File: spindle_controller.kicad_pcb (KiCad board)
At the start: 2 copper layers, 62 x 112 mm, 67 parts, among them J1 VAC 230V, J2 AUX/CONTROL, J3 ICP, J4 Load output, J5 CONN_01X03, J6 CONN_01X03, J7 GND_JUMPER, J8 VCC_JUMPER, Q1 2N3904, SW1 Rotary_Encoder_Switch, T1 230 - 6VAC (Spitznagel SPK 01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, U1 LM2940CT-5.0, U2 ATMEGA328P-PU, U3 PC817, U4 MOC3020M, U5 TCRT5000, U6 LT1117-5, Y1 16MHz

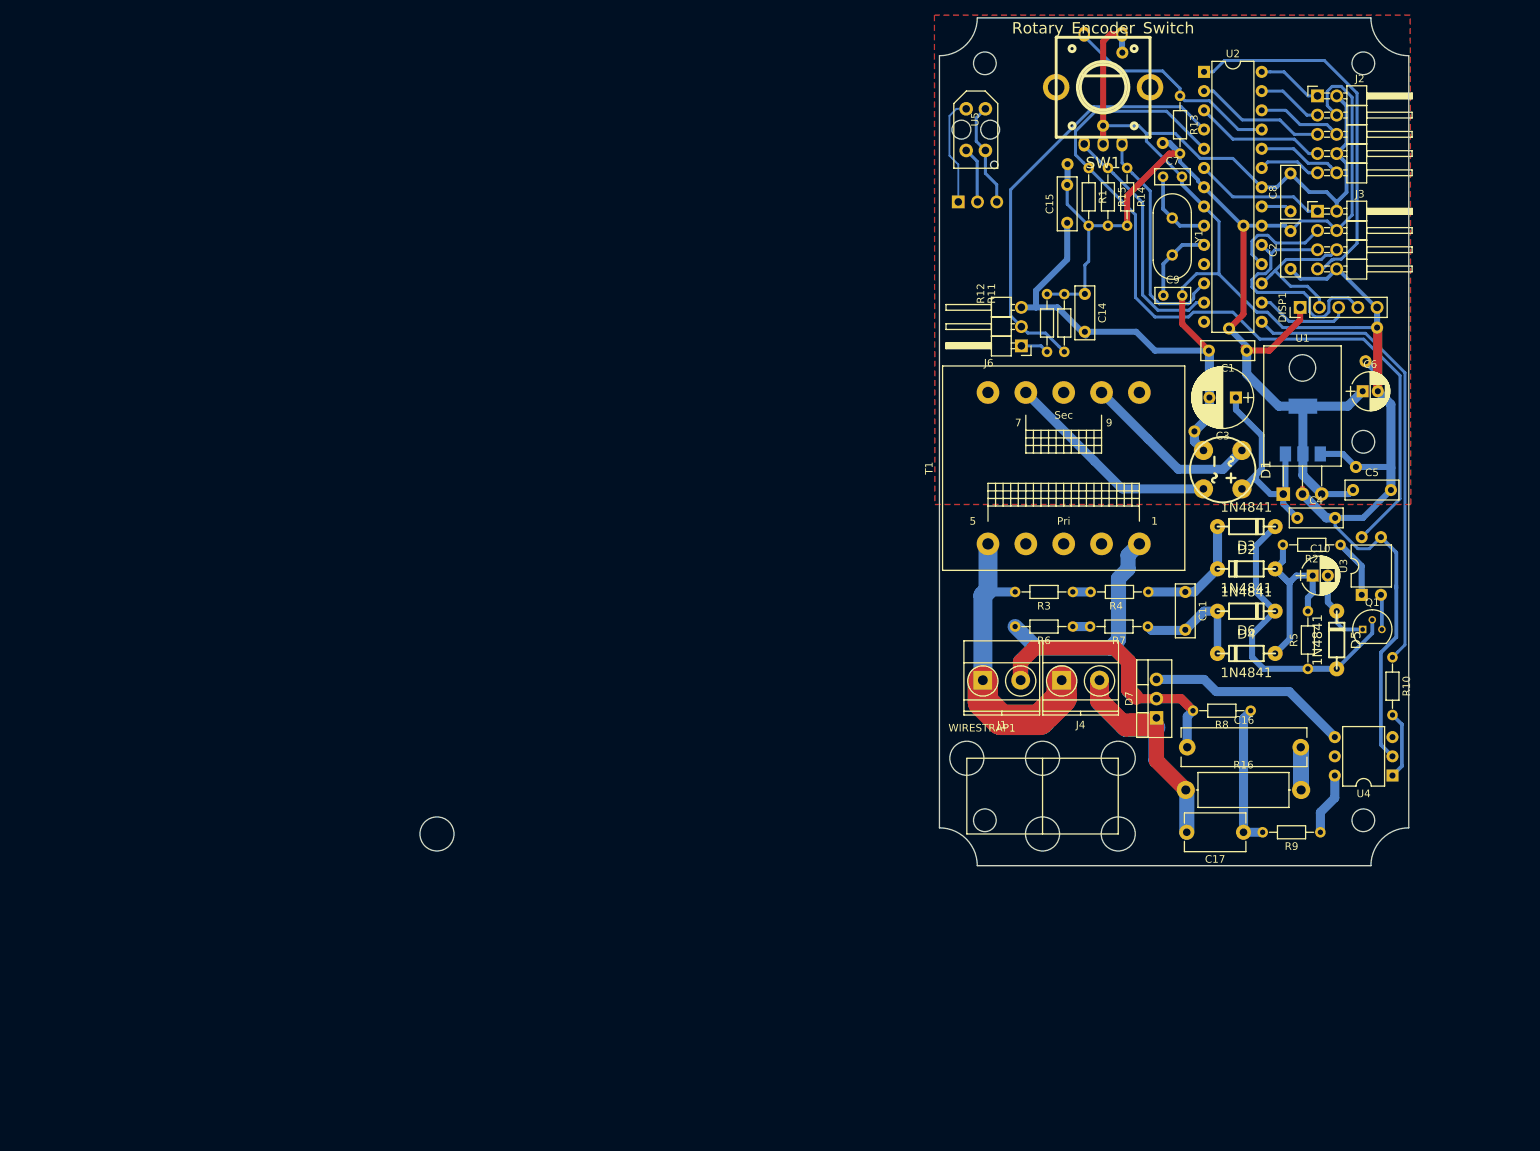
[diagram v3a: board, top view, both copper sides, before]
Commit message: Add breakaway board for optical sensor, general board updates, dissipation planes, screw clearances and silkscreen
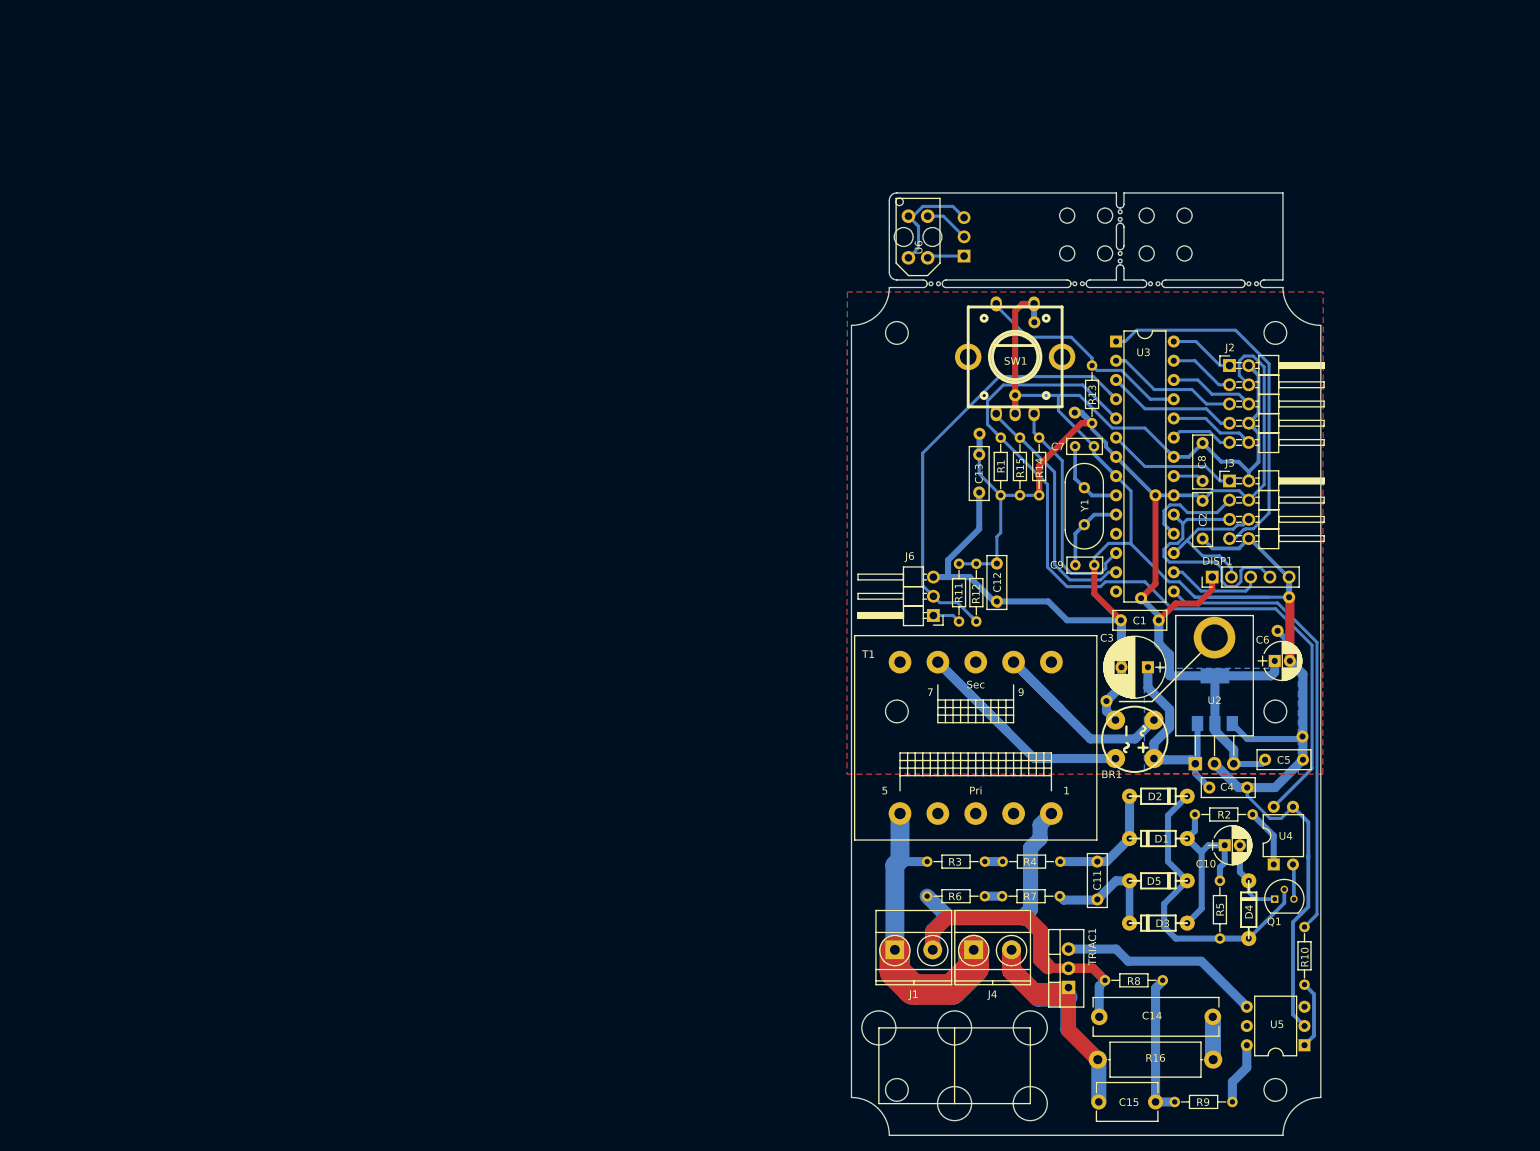
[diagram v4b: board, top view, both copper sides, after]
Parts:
- removed the U1 at (115.9, 77.4)
- added U2: LM2940CT-5.0, iotta_footprints:TO-220_Horizontal_connected_tab, F.Cu at (104.3, 113.0)
- CASE1: footprint iotta_footprints:CASE_KEMO_G085N -> iotta_footprints:CASE_KEMO_G085N+BREAKAWAY_SENSOR
- WIRESTRAP1: footprint iotta_footprints:WireStrap_2X -> iotta_footprints:WireStrap_2X_5HOLES
- moved C11 37.5 mm to (91.3, 125.9)
- moved C14 37.5 mm to (91.6, 146.4)
- moved C15 37.5 mm to (99.0, 157.7)
- moved C2 37.5 mm to (105.2, 83.2)
- moved C3 37.5 mm to (98.0, 100.2)
- moved C5 37.5 mm to (113.5, 112.5)
- moved CASE1 37.5 mm to (54.8, 166.1)
- moved D1 37.5 mm to (99.4, 122.9)
- moved DISP1 37.5 mm to (106.5, 88.3)
- moved J1 37.5 mm to (64.6, 137.6)
- moved J4 37.5 mm to (75.0, 137.6)
- moved J6 37.5 mm to (69.7, 93.4)
- moved J7 37.5 mm to (92.5, 104.7)
- moved J7 37.5 mm to (116.6, 91.0)
- moved J7 37.5 mm to (80.5, 64.3)
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- renumbered D1 to BR1, C14 to C12, C15 to C13, C16 to C14, C17 to C15, D2 to D1, D3 to D2, D4 to D3, D5 to D4, D6 to D5, D7 to TRIAC1, U6 to U1, U2 to U3, U3 to U4, U4 to U5, U5 to U6
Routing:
- net Net-(BR1-Pad3): track 28.7 -> 41.6 mm
- net GND: track 307.7 -> 319.2 mm
- net Net-(J5-Pad1): track 14.4 -> 4.91 mm
- net Net-(BR1-Pad2): track 23.8 -> 32.5 mm
- net /ZCROSS_PULSE: track 108.6 -> 114.2 mm
- net Net-(J5-Pad3): track 13.9 -> 18.2 mm
- net VCC: track 166.7 -> 169.7 mm
- net /VAC_L: track 95.5 -> 98.4 mm
- net /ROT_PULSE: track 57.1 -> 59.6 mm
- net Net-(C15-Pad2): track 80.3 -> 82.1 mm
- net /MOSI: track 20.3 -> 22.0 mm
- net Net-(J5-Pad2): track 7.44 -> 5.94 mm
- net /TRIAC_DRIVE: track 60.0 -> 61.3 mm
- net /PC3: track 11.2 -> 12.4 mm
- net /PD7: track 11.2 -> 12.4 mm
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- added copper zone on B.Cu, net VCC
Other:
- board size 62 x 112 mm -> 62 x 124.5 mm
- board text removed: "Liggende TO220 voor 7805. screw to board, sink via's Angled connectors aan achterkant huis INpassen sensor break-off board. Aanpassen C17 footpirnt naar Y2 ceramic"

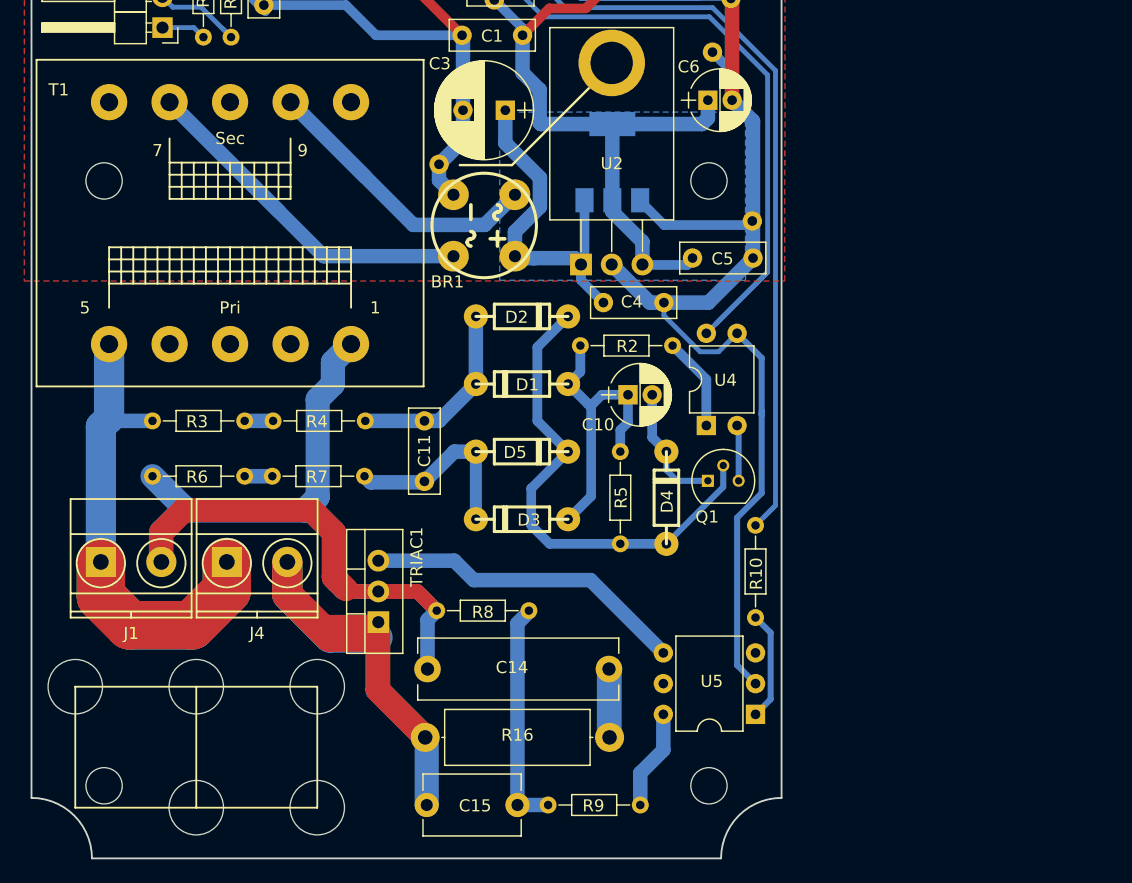
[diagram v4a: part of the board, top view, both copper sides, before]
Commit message: Trying to __squeeze__ in a heatsink for the TRIAC, routing suffers.
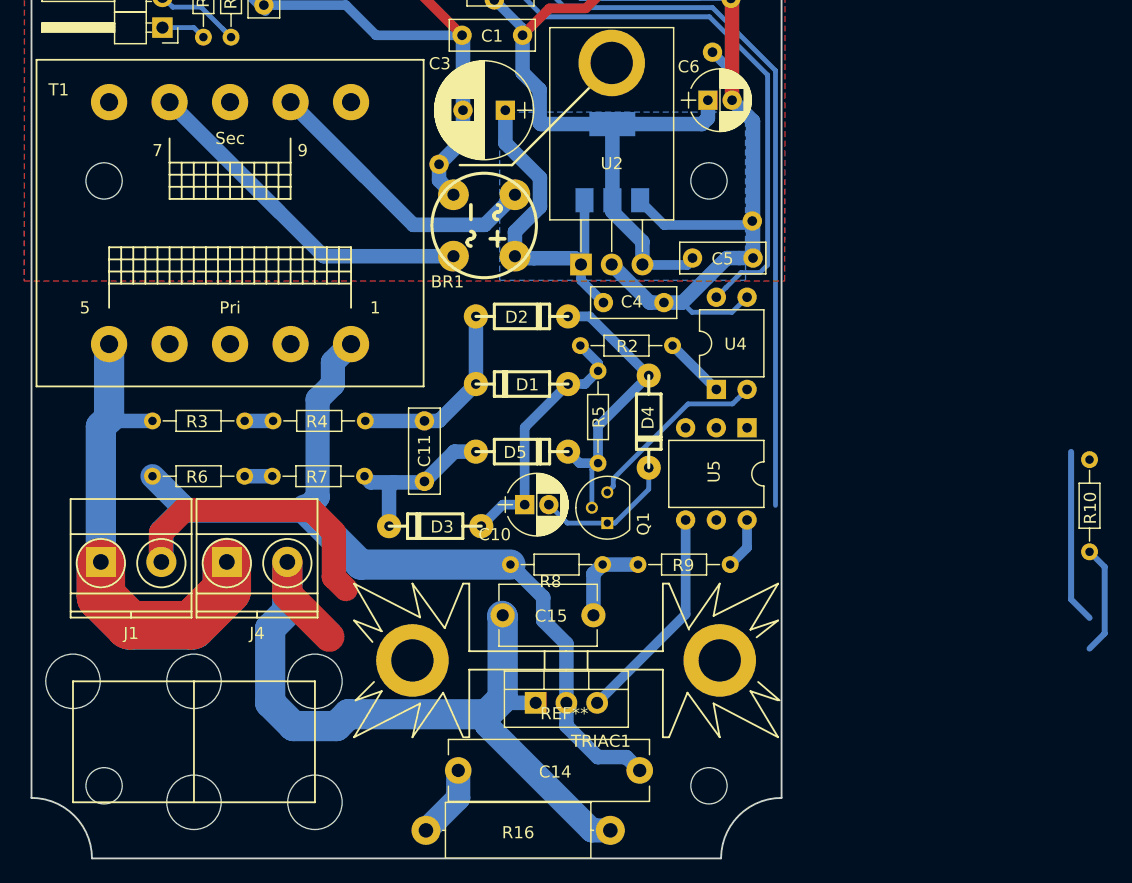
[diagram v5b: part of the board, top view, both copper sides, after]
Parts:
- added REF**: Heatsink_Fischer_SK104-STCB_35x13mm__2xDrill3.5mm_ScrewM3, Heatsinks:Heatsink_Fischer_SK104-STCB_35x13mm__2xDrill3.5mm_ScrewM3, F.Cu at (103.0, 145.7)
- moved R10 28.1 mm to (146.3, 129.1)
- moved U5 23.7 mm to (118.0, 126.5), turned to 270 degrees
- moved R9 21.2 mm to (116.6, 137.8)
- moved C14 19.4 mm to (109.1, 154.8), turned to 180 degrees
- moved R16 17.1 mm to (106.7, 159.8), turned to 180 degrees
- moved C15 16.9 mm to (105.3, 142.0)
- moved TRIAC1 14.6 mm to (100.5, 149.2), turned to 0 degrees
- moved C10 12.5 mm to (99.6, 132.8)
- moved Q1 9.02 mm to (106.4, 134.4), turned to 90 degrees
- moved D3 7.20 mm to (92.2, 134.6)
- moved R8 7.19 mm to (106.0, 137.8)
- moved R5 6.92 mm to (105.7, 129.4)
- moved D4 6.45 mm to (109.9, 126.0), turned to 270 degrees
- moved U4 3.10 mm to (115.4, 123.3)
- moved WIRESTRAP1 0.48 mm to (72.3, 147.4)
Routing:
- net GND: track 319.2 -> 280.4 mm
- net Net-(D2-Pad2): track 40.9 -> 24.4 mm
- net (no net): track 0.00 -> 14.3 mm
- net Net-(C15-Pad1): track 19.0 -> 7.43 mm
- net Net-(Q1-Pad3): track 4.62 -> 15.5 mm
- net Net-(C15-Pad2): track 82.1 -> 73.3 mm
- net Net-(TRIAC1-Pad3): track 26.7 -> 18.1 mm
- net /ZCROSS_PULSE: track 114.2 -> 105.7 mm
- net Net-(C10-Pad1): track 27.3 -> 21.4 mm
- net Net-(C14-Pad2): track 11.3 -> 6.06 mm
- net Net-(R9-Pad1): track 8.28 -> 4.26 mm
- net /TRIAC_DRIVE: track 61.3 -> 57.7 mm
- net Net-(R2-Pad1): track 7.76 -> 5.12 mm
- net Net-(C11-Pad2): track 16.1 -> 14.2 mm
- net Net-(C10-Pad2): track 10.5 -> 11.8 mm
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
